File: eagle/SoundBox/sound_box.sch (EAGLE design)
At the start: 24 parts, among them IC1 7805T, J1 DCJ0202, X1 PN61729-S

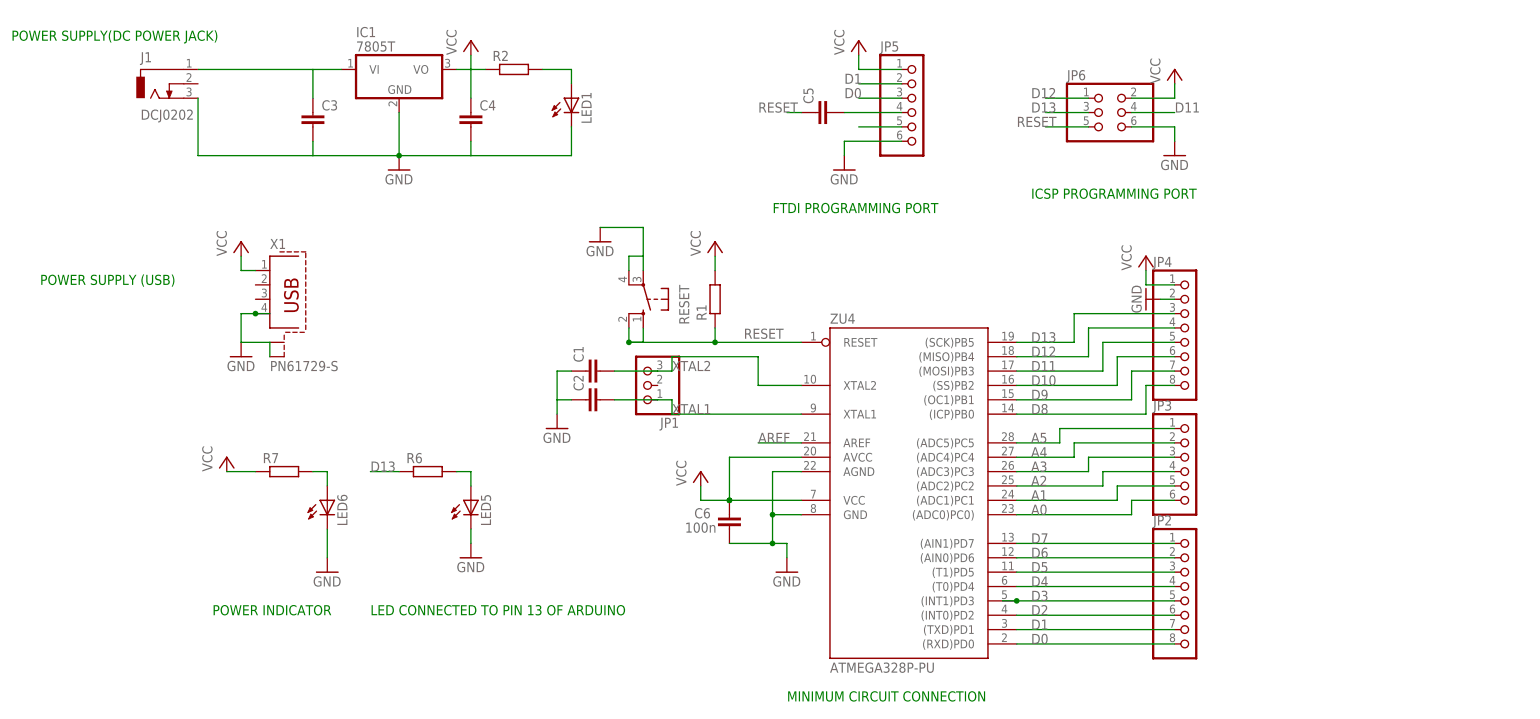
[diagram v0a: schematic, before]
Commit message: adding non-standard eagle libraries, attiny13 arduino IDE support files, and sound box schematic. Also electromagnet project changes
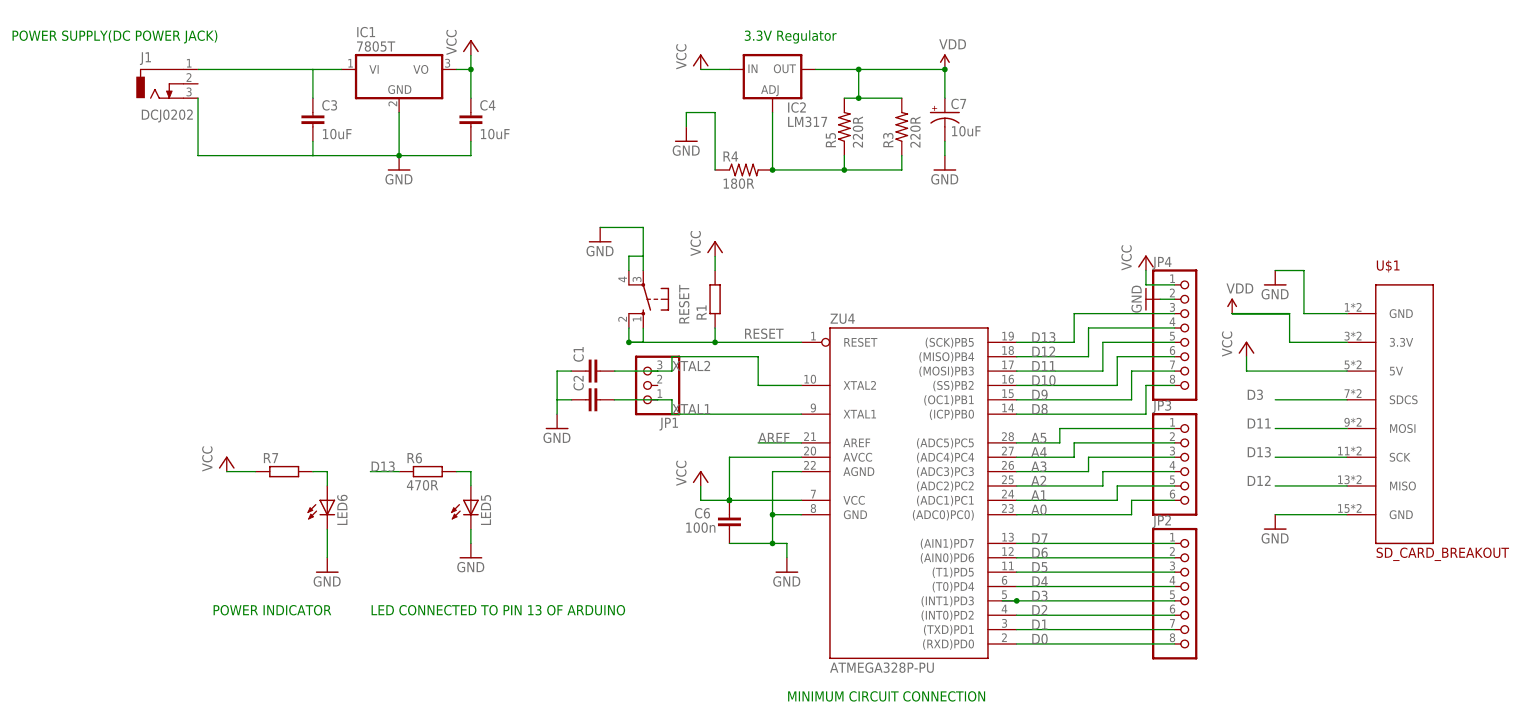
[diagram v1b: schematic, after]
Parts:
- removed C5: (no value), capacitor-wima:C2.5/5
- removed JP5: (no value), pinhead:PINHD-1X6
- removed JP6: (no value), pinhead:PINHD-2X3
- removed LED1: (no value), led:LED5MM
- removed R2: (no value), rcl:R-EU_0207/10
- removed X1: PN61729-S, con-berg:PN61729-S
- added C7: 10uF, rcl:CPOL-USE2.5-5
- added IC2: LM317, v-reg:LM317TS
- added R3, R5: 220R, rcl:R-US_0204/7
- added R4: 180R, rcl:R-US_0204/7
- added U$1: SD_CARD_BREAKOUT, sd_card_breakout:SD_CARD_BREAKOUT
- C3, C4: value (none) -> 10uF
- R6: value (none) -> 470R
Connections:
- removed net N$15: C5.2, JP5.4
- removed net N$16: JP5.5
- removed net N$6: LED1.A, R2.2
- new net N$1: IC2.ADJ, R3.1, R4.2, R5.1
- new net VDD: C7.+, IC2.OUT, R3.2, R5.2, U$1.3.3V
- net D0: no longer JP5.3
- net D1: no longer JP5.2
- net D11: now also U$1.MOSI; no longer JP6.4
- net D12: now also U$1.MISO; no longer JP6.1
- net D13: now also U$1.SCK; no longer JP6.3
- net D3: now also U$1.SDCS
- net GND: now also C7.-, R4.1, U$1.GND@1, U$1.GND@2; no longer JP5.6, JP6.6, LED1.C, X1.4, X1.S1, X1.S2
- net RESET: no longer C5.1, JP6.5
- net VCC: now also IC2.IN, U$1.5V; no longer JP5.1, JP6.2, R2.1, X1.1
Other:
- note added: "3.3V Regulator"
- note removed: "FTDI PROGRAMMING PORT"
- note removed: "ICSP PROGRAMMING PORT"
- note removed: "POWER SUPPLY (USB)"

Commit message: finished sound box schematic
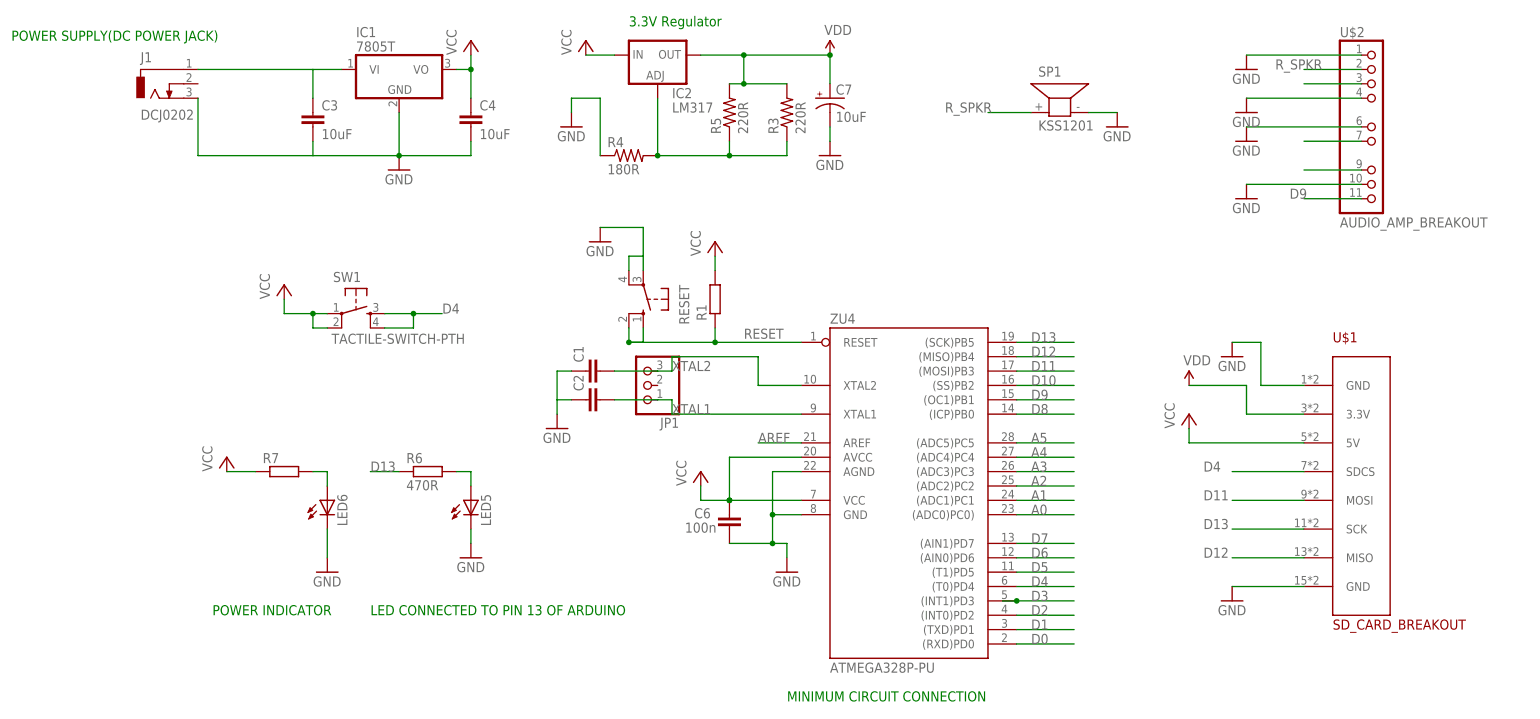
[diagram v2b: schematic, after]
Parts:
- removed JP2, JP4: (no value), pinhead:PINHD-1X8
- removed JP3: (no value), pinhead:PINHD-1X6
- added SP1: KSS1201, buzzer:KSS1201
- added SW1: TACTILE-SWITCH-PTH, GeekAmmo:TACTILE-SWITCH-PTH
- added U$2: AUDIO_AMP_BREAKOUT, audio_amp_breakout:AUDIO_AMP_BREAKOUT
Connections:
- new net N$11: U$2.POW_POS
- new net N$12: U$2.L_INPUT
- new net N$6: U$2.L_OUT_POS
- new net R_SPKR: SP1.1, U$2.R_OUT_POS
- net A0: no longer JP3.6
- net A1: no longer JP3.5
- net A2: no longer JP3.4
- net A3: no longer JP3.3
- net A4: no longer JP3.2
- net A5: no longer JP3.1
- net D0: no longer JP2.8
- net D1: no longer JP2.7
- net D10: no longer JP4.6
- net D11: no longer JP4.5
- net D12: no longer JP4.4
- net D13: no longer JP4.3
- net D2: no longer JP2.6
- net D3: no longer JP2.5, U$1.SDCS
- net D4: now also SW1.3, SW1.4, U$1.SDCS; no longer JP2.4
- net D5: no longer JP2.3
- net D6: no longer JP2.2
- net D7: no longer JP2.1
- net D8: no longer JP4.8
- net D9: now also U$2.R_INPUT; no longer JP4.7
- net GND: now also SP1.2, U$2.GND@1, U$2.GND@2, U$2.GND@3, U$2.GND@4; no longer JP4.2
- net VCC: now also SW1.1, SW1.2; no longer JP4.1
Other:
- moved on the sheet: C7, IC2, R3, R4, R5, U$1
